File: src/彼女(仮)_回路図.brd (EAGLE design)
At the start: 65.7 x 50 mm, 55 parts, among them IC1 A3921, SW1 TVAF06-A020B-R, SW2 TVAF06-A020B-R, SW3 THAF01-NC-R, SW4 SS-12D00G3

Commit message: first commit
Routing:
- net SA: track 1.81 -> 17.1 mm
- net V5: track 48.1 -> 50.5 mm
- net GND: track 23.3 -> 25.4 mm
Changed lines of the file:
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@@
 <wire x1="49.22" y1="30.84" x2="49.22" y2="31.84" width="0.1524" layer="16"/>
 <wire x1="49.22" y1="30.84" x2="48.98" y2="30.6" width="0.1524" layer="16"/>
+<wire x1="35.84" y1="29.68" x2="35.84" y2="31.7" width="0.1524" layer="16"/>
+<wire x1="35.84" y1="31.7" x2="35.78" y2="31.76" width="0.1524" layer="16"/>
 <wire x1="49.99" y1="38.87" x2="55.8" y2="39.2" width="0" layer="19" extent="16-16"/>
 <wire x1="50.69" y1="44.2" x2="49.99" y2="38.87" width="0" layer="19" extent="16-16"/>
@@
 <wire x1="42.34" y1="23.58" x2="45.11" y2="27.28" width="0" layer="19" extent="1-16"/>
 <wire x1="35.78" y1="31.76" x2="42.68" y2="31.84" width="0" layer="19" extent="16-16"/>
-<wire x1="35.84" y1="29.68" x2="35.78" y2="31.76" width="0" layer="19" extent="16-16"/>
 <wire x1="41.77" y1="39.2" x2="42.68" y2="31.84" width="0" layer="19" extent="16-16"/>
 <wire x1="45.54" y1="4.35" x2="41.7" y2="21.3" width="0" layer="19" extent="16-16"/>
@@
 <wire x1="47.3" y1="32.9" x2="42.34" y2="32.9" width="0.1524" layer="16"/>
 <wire x1="42.34" y1="32.9" x2="41.28" y2="31.84" width="0.1524" layer="16"/>
+<wire x1="37.79" y1="29.68" x2="37.79" y2="31.15" width="0.1524" layer="16"/>
+<wire x1="37.79" y1="31.15" x2="37.18" y2="31.76" width="0.1524" layer="16"/>
 <wire x1="47.82" y1="31.84" x2="55.59" y2="26.01" width="0" layer="19" extent="1-16"/>
 <wire x1="40.61" y1="31.81" x2="41.28" y2="31.84" width="0" layer="19" extent="1-16"/>
@@
 <wire x1="38.44" y1="29.68" x2="39.09" y2="29.68" width="0" layer="19" extent="16-16"/>
 <wire x1="37.79" y1="29.68" x2="38.44" y2="29.68" width="0" layer="19" extent="16-16"/>
-<wire x1="37.18" y1="31.76" x2="37.79" y2="29.68" width="0" layer="19" extent="16-16"/>
 <wire x1="6.59" y1="34.66" x2="37.18" y2="31.76" width="0" layer="19" extent="16-16"/>
 <wire x1="4.41" y1="34.7" x2="6.59" y2="34.66" width="0" layer="19" extent="16-16"/>
@@
 <contactref element="EDGE1" pad="P$3"/>
 <contactref element="EDGE1" pad="P$4"/>
-<wire x1="36.42" y1="21.8" x2="36.42" y2="23.51" width="0.1524" layer="16"/>
+<wire x1="36.42" y1="23.51" x2="36.42" y2="21.8" width="0.1524" layer="16"/>
 <wire x1="36.42" y1="23.51" x2="36.49" y2="23.58" width="0.1524" layer="16"/>
+<wire x1="36.42" y1="21.8" x2="36.42" y2="19.29" width="0.1524" layer="16"/>
+<wire x1="36.42" y1="19.29" x2="35.78" y2="18.65" width="0.1524" layer="16"/>
+<wire x1="35.78" y1="18.65" x2="29.52" y2="18.65" width="0.1524" layer="16"/>
+<wire x1="29.52" y1="18.65" x2="25.58" y2="22.59" width="0.1524" layer="16"/>
 <wire x1="24.29" y1="28.75" x2="11.71" y2="45.72" width="0" layer="19" extent="16-16"/>
 <wire x1="25.58" y1="22.59" x2="24.29" y2="28.75" width="0" layer="19" extent="16-16"/>
-<wire x1="36.42" y1="21.8" x2="25.58" y2="22.59" width="0" layer="19" extent="16-16"/>
 <wire x1="12.59" y1="14.7546" x2="25.58" y2="22.59" width="0" layer="19" extent="1-16"/>
 <wire x1="12.52" y1="4.35" x2="12.59" y2="14.7546" width="0" layer="19" extent="1-16"/>

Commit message: brd編集 配線
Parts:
- moved 3813-HA 4.00 mm to (22.8, 23.7)
- moved 3813-LA 4.00 mm to (8.59, 23.7)
- moved C10 2.00 mm to (39.8, 41.7)
- moved C7 1.30 mm to (40.4, 22.2), flipped to the bottom, turned to 180 degrees
- moved 3813-HB 1.00 mm to (25.3, 33.8)
- moved 3813-LB 1.00 mm to (11.1, 33.8)
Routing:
- net N$11: track 0.00 -> 23.2 mm
- net V5: track 50.5 -> 73.6 mm, vias 2 -> 3
- net SA: track 17.1 -> 1.81 mm
- net GND: track 25.4 -> 33.9 mm
- net N$3: track 0.00 -> 5.76 mm, vias 0 -> 1
- net N$4: track 0.00 -> 5.73 mm
- net N$2: track 0.00 -> 4.73 mm
- net N$1: track 0.00 -> 2.46 mm
- net N$15: track 3.11 -> 1.46 mm, vias 1 -> 0
- net SB: track 3.09 -> 1.44 mm, vias 1 -> 0
- net PWM: track 28.6 -> 29.9 mm
- net N$25: track 0.00 -> 0.61 mm

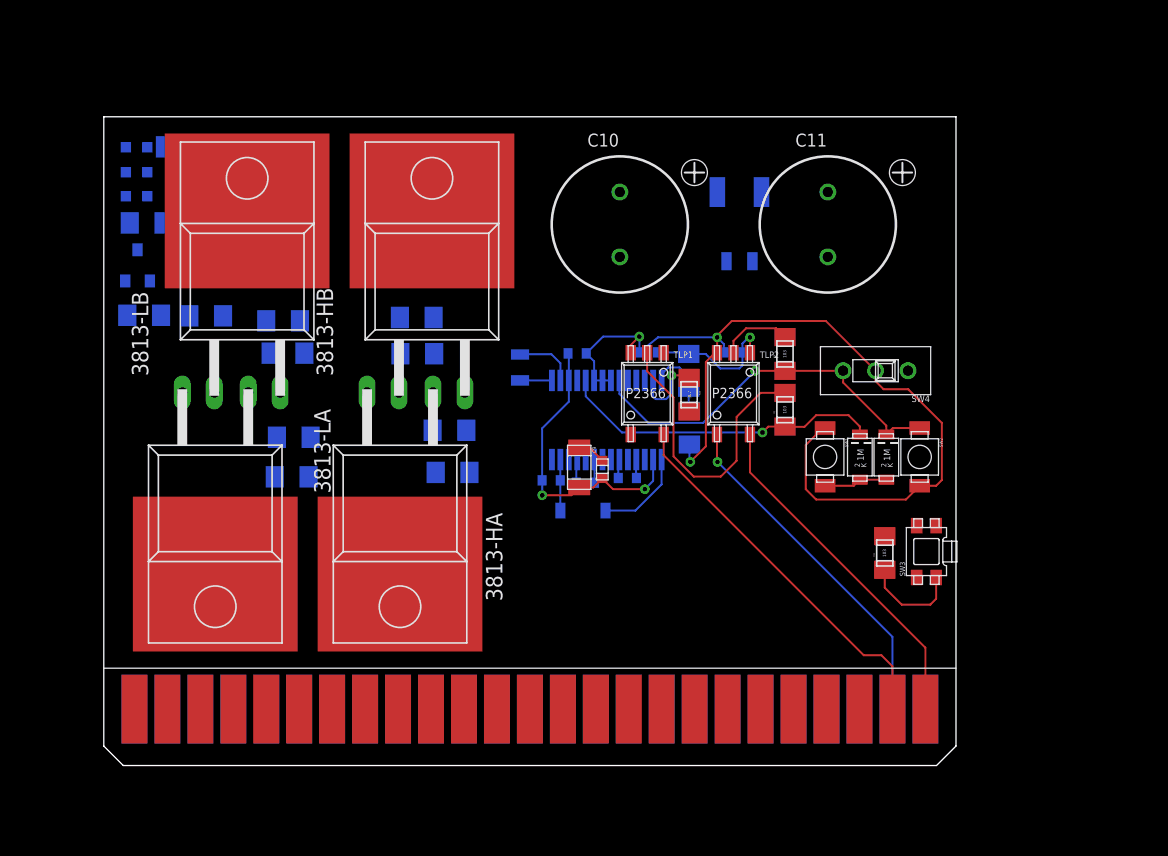
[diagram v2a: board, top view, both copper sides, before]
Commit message: 部品配置訂正 大電流パターン考慮
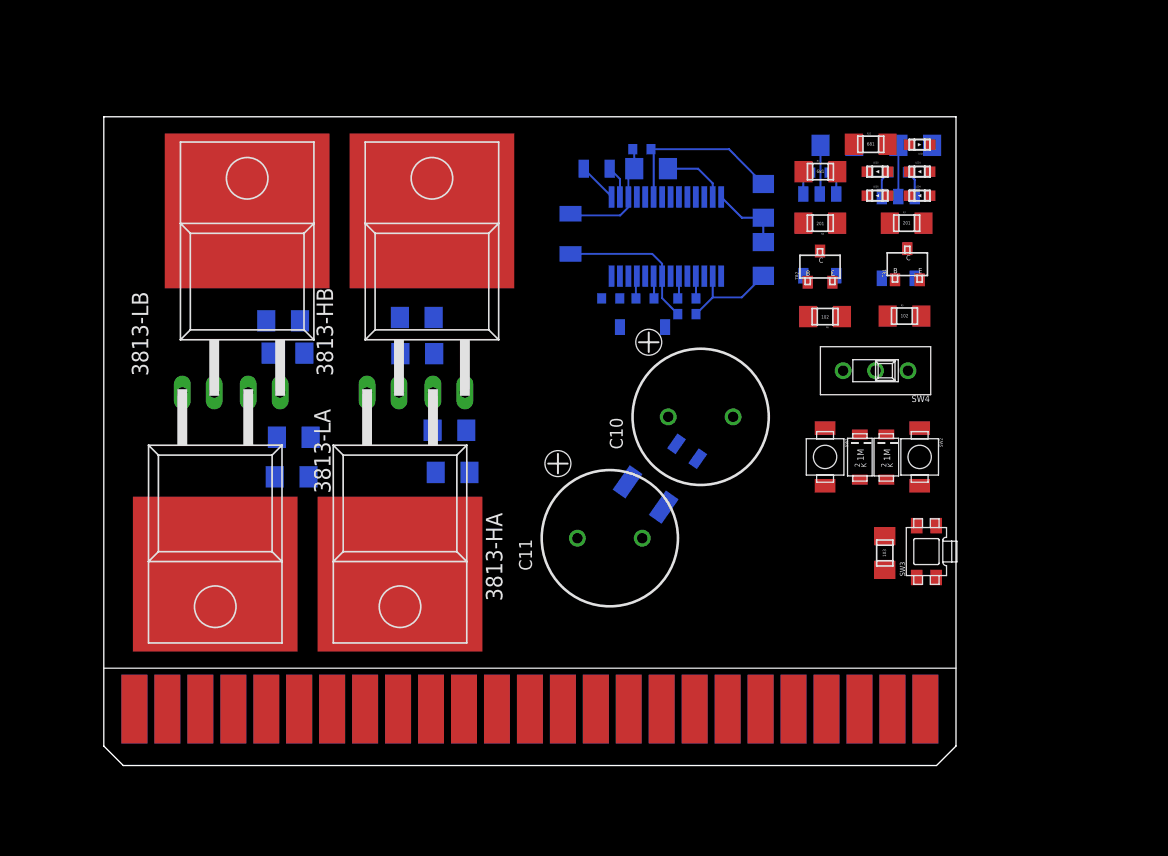
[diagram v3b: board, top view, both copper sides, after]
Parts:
- moved LED3 62.0 mm to (63.7, 47.9), flipped to the top
- moved LED1 60.4 mm to (62.0, 45.8), flipped to the top, turned to 270 degrees
- moved TR1 57.3 mm to (62.9, 37.4), flipped to the top
- moved LED5 57.1 mm to (58.8, 43.9), flipped to the top, turned to 270 degrees
- moved LED4 56.5 mm to (62.0, 43.9), flipped to the top, turned to 270 degrees
- moved TR2 54.5 mm to (56.1, 37.2), flipped to the top
- moved R7 54.4 mm to (60.6, 41.8), flipped to the top, turned to 0 degrees
- moved R5 53.8 mm to (60.4, 34.6), flipped to the top, turned to 0 degrees
- moved LED2 53.3 mm to (58.8, 45.8), flipped to the top, turned to 270 degrees
- moved R6 52.5 mm to (56.9, 34.6), flipped to the top, turned to 180 degrees
- moved R8 51.9 mm to (56.5, 41.8), flipped to the top, turned to 180 degrees
- moved R22 50.5 mm to (57.8, 47.9), flipped to the top
- moved R3 42.2 mm to (53.9, 45.8), flipped to the top
- moved C11 29.4 mm to (39.0, 17.5), turned to 90 degrees
- moved TLP1 25.0 mm to (62.5, 37.5), flipped to the bottom
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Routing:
- net V5: track 73.6 -> 17.5 mm, vias 3 -> 0
- net PWM: track 29.9 -> 0.00 mm, vias 1 -> 0
- net GND_IN: track 29.3 -> 0.00 mm
- net VCC_IN: track 26.8 -> 0.00 mm, vias 1 -> 0
- net PWM_IN: track 26.8 -> 0.00 mm
- net DIR: track 25.1 -> 0.00 mm, vias 1 -> 0
- net N$11: track 23.2 -> 3.95 mm
- net GND: track 33.9 -> 21.5 mm, vias 3 -> 0
- net N$6: track 2.20 -> 11.8 mm
- net RESET: track 7.70 -> 0.00 mm
- net VCC: track 7.07 -> 0.00 mm
- net N$12: track 4.91 -> 0.00 mm
- net N$7: track 3.94 -> 0.00 mm
- net N$2: track 4.73 -> 2.51 mm
- net N$14: track 5.57 -> 3.77 mm
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
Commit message: edit:配線の追加
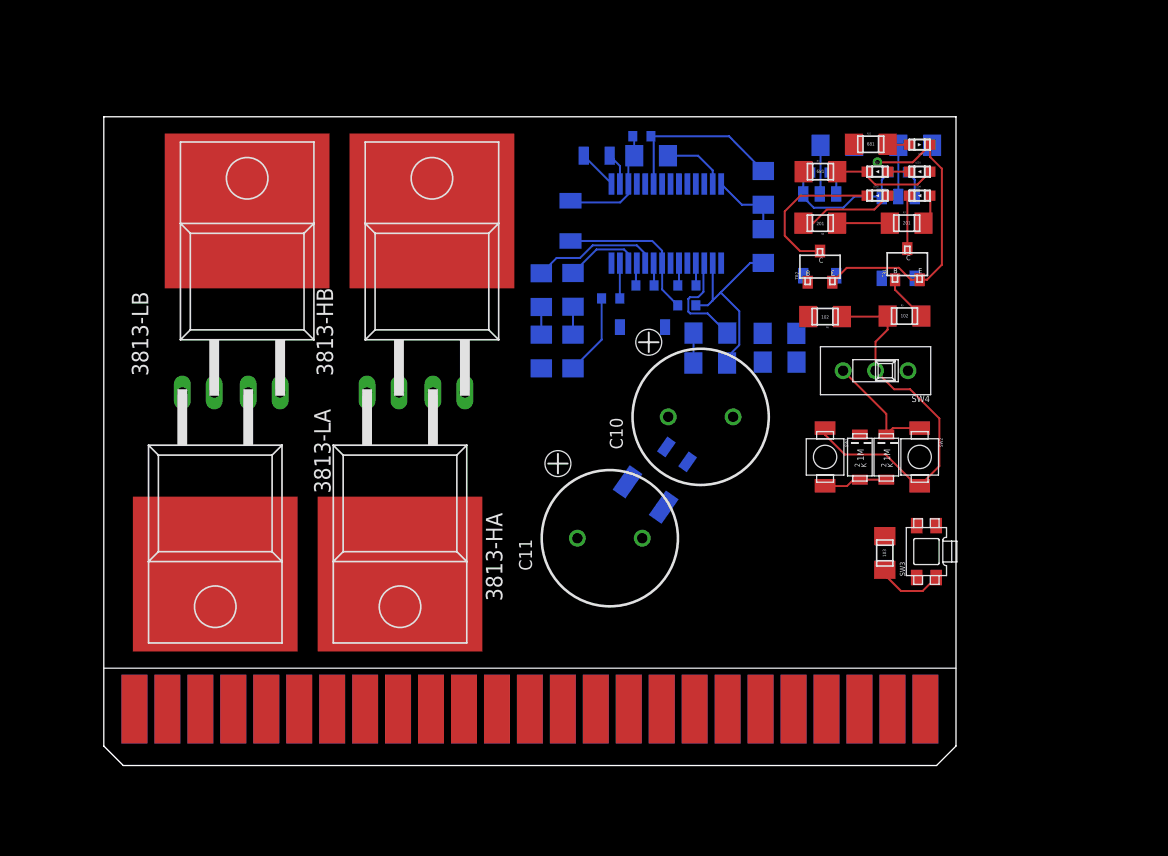
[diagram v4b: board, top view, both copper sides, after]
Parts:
- moved R18 33.1 mm to (48.0, 31.0)
- moved R10 32.6 mm to (48.0, 33.3)
- moved R19 28.2 mm to (53.4, 31.1)
- moved R12 28.0 mm to (53.4, 33.3)
- moved R20 24.9 mm to (36.2, 35.4), turned to 90 degrees
- moved R15 24.5 mm to (36.2, 30.6), turned to 90 degrees
- moved R21 12.7 mm to (33.7, 35.3), turned to 90 degrees
- moved R16 11.4 mm to (33.7, 30.6), turned to 90 degrees
- moved C3 1.00 mm to (41.5, 48.5)
- moved C6 1.00 mm to (38.0, 47.0)
- moved C7 1.00 mm to (44.9, 37.0)
- moved C8 1.00 mm to (41.7, 37.0)
- moved C9 1.00 mm to (36.0, 42.0)
- moved IC1 1.00 mm to (47.6, 39.6)
- moved R13 1.00 mm to (43.5, 47.0)
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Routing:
- net GND: track 21.5 -> 67.9 mm, vias 0 -> 1
- net V5: track 17.5 -> 51.4 mm
- net N$8: track 0.00 -> 11.9 mm
- net GHA: track 0.00 -> 9.89 mm
- net PWM: track 0.00 -> 9.08 mm
- net GLB: track 0.00 -> 8.56 mm
- net N$18: track 0.00 -> 8.19 mm
- net N$10: track 0.00 -> 7.41 mm
- net GLA: track 0.00 -> 5.88 mm
- net RESET: track 0.00 -> 5.29 mm
- net N$12: track 0.00 -> 5.26 mm
- net N$5: track 0.00 -> 4.13 mm
- net N$19: track 0.00 -> 3.64 mm
- net N$7: track 0.00 -> 2.72 mm
- net N$9: track 0.00 -> 2.34 mm
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
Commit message: edit:GND,VCCベタ,wireの追加
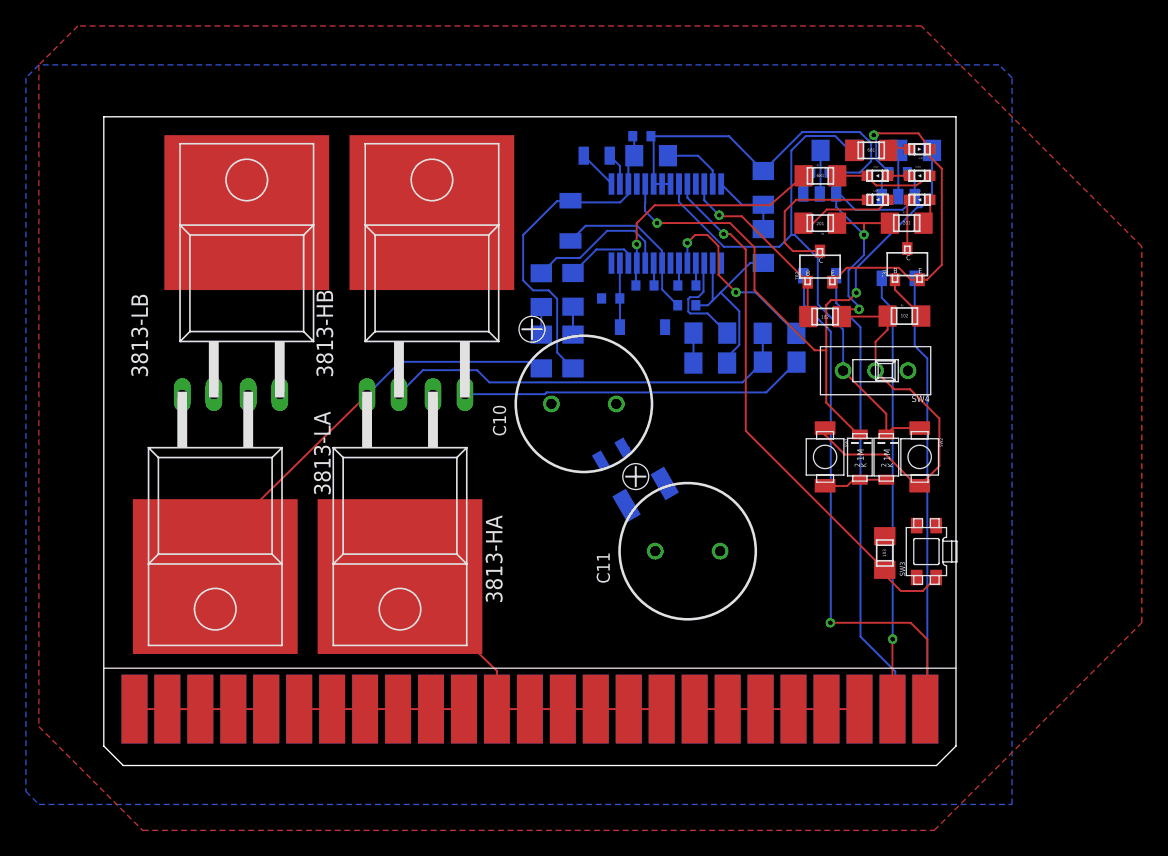
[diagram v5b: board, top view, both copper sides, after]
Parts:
- moved C10 9.06 mm to (37.0, 27.9)
- moved C11 6.08 mm to (45.0, 16.5)
- moved C13 5.00 mm to (39.2, 24.0), turned to 150 degrees
- moved R22 0.47 mm to (57.9, 47.4)
- moved R1 0.39 mm to (63.8, 47.4)
- moved R9 0.39 mm to (57.8, 47.4)
- moved LED3 0.35 mm to (63.7, 47.5)
- moved LED5 0.32 mm to (58.8, 43.6)
- moved LED1 0.32 mm to (62.0, 45.5)
- moved LED2 0.32 mm to (58.8, 45.5)
- moved LED4 0.32 mm to (62.0, 43.6)
- moved R3 0.32 mm to (53.9, 45.5)
- moved 3813-HA 0.19 mm to (22.8, 23.5)
- moved 3813-LA 0.19 mm to (8.59, 23.5)
- moved 3813-LB 0.13 mm to (11.0, 33.7)
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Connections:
- removed net N$19: R5.RIGHT, TR1.B
- removed net N$20: R6.RIGHT, TR2.B
- net FF1: now also R5.RIGHT, TR1.B
- net FF2: now also R6.RIGHT, TR2.B
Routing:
- net SA: track 1.75 -> 62.9 mm, vias 0 -> 1
- net DIR: track 0.00 -> 49.9 mm, vias 0 -> 2
- net PWM_IN: track 0.00 -> 43.4 mm, vias 0 -> 1
- net SB: track 3.32 -> 42.6 mm
- net V5: track 51.4 -> 87.8 mm, vias 0 -> 2
- net RESET: track 5.29 -> 41.6 mm, vias 0 -> 1
- net PWM: track 9.08 -> 45.4 mm
- net VCC_IN: track 0.00 -> 35.4 mm
- net DIR_IN: track 0.00 -> 33.7 mm
- net GND_IN: track 0.00 -> 33.6 mm, vias 0 -> 1
- net N$21: track 0.00 -> 32.1 mm
- net VCC: track 0.30 -> 26.1 mm
- net GND: track 67.9 -> 89.9 mm
- net GHB: track 0.00 -> 14.7 mm, vias 0 -> 2
- net FF2: track 0.00 -> 14.6 mm, vias 0 -> 1
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- added copper zone on layer 16, net GND
- added copper zone on layer 1, net VCC

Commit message: edit:大体配線完了
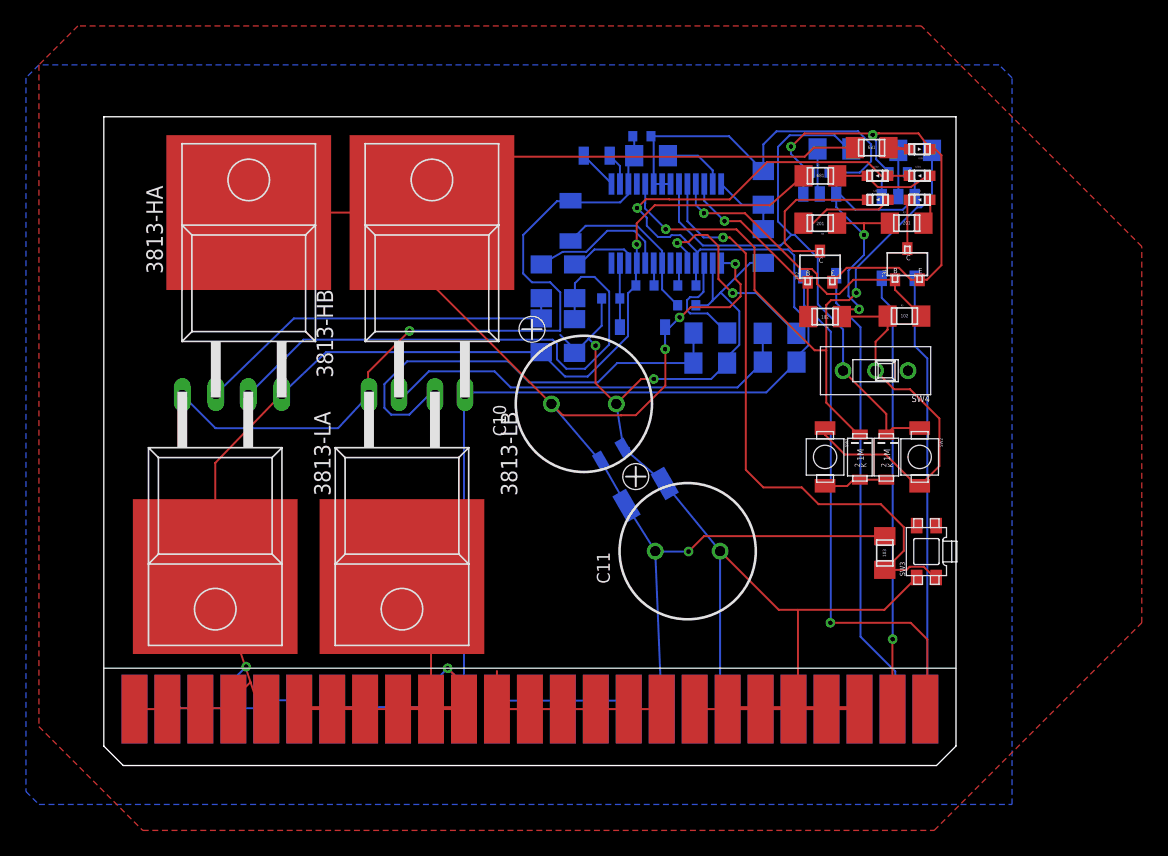
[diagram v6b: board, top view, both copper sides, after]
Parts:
- moved 3813-LB 15.7 mm to (23.0, 23.5), turned to 180 degrees
- moved 3813-HA 15.5 mm to (11.2, 33.7), turned to 0 degrees
- moved R16 1.25 mm to (33.7, 31.9)
- moved R15 1.20 mm to (36.3, 31.8)
- moved R21 0.68 mm to (33.7, 36.0)
- moved R20 0.67 mm to (36.3, 36.0)
- moved R9 0.25 mm to (57.6, 47.5)
- moved R22 0.21 mm to (57.9, 47.6)
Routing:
- net VCC: track 26.1 -> 179.6 mm, vias 0 -> 4
- net GND: track 89.9 -> 229.0 mm, vias 1 -> 5
- net SB: track 42.6 -> 154.0 mm, vias 0 -> 2
- net SA: track 62.9 -> 115.2 mm, vias 1 -> 2
- net N$25: track 2.15 -> 42.2 mm
- net N$26: track 2.31 -> 34.7 mm
- net N$13: track 2.13 -> 29.0 mm
- net FF1: track 3.64 -> 24.3 mm, vias 0 -> 1
- net RESET: track 41.6 -> 47.8 mm
- net PWM: track 45.4 -> 47.6 mm
- net V5: track 87.8 -> 89.6 mm
- net N$22: track 1.62 -> 3.29 mm
- net GHB: track 14.7 -> 16.0 mm

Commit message: ビアの配置
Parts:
- moved 3813-HA 1.10 mm to (11.2, 34.8)
- moved 3813-HB 1.10 mm to (25.3, 34.8)
- moved 3813-LA 1.08 mm to (8.59, 24.6)
- moved 3813-LB 1.08 mm to (23.0, 24.6)
- moved R18 1.00 mm to (48.0, 32.0)
- moved R19 1.00 mm to (53.4, 32.1)
- moved C1 1.00 mm to (61.2, 46.7)
- moved C10 1.00 mm to (37.0, 28.9)
- moved C11 1.00 mm to (45.0, 17.5)
- moved C12 1.00 mm to (41.8, 21.9)
- moved C13 1.00 mm to (39.2, 25.0)
- moved C2 1.00 mm to (55.2, 46.7)
- moved C3 1.00 mm to (41.5, 49.5)
- moved C4 1.00 mm to (44.9, 36.5)
- moved C5 1.00 mm to (39.1, 37.0)
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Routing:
- net SA: track 115.2 -> 53.4 mm, vias 2 -> 123
- net SB: track 154.0 -> 98.1 mm, vias 2 -> 1
- net GND: track 229.0 -> 173.4 mm
- net VCC: track 179.6 -> 125.6 mm
- net VCC_IN: track 35.4 -> 36.4 mm
- net PWM_IN: track 43.4 -> 44.4 mm
- net GND_IN: track 33.6 -> 34.6 mm
- net DIR_IN: track 33.7 -> 34.7 mm
- net N$26: track 34.7 -> 35.3 mm
- added copper zone on layer 1, net SA
- added copper zone on layer 16, net SA
- added copper zone on layer 1, net SB
- added copper zone on layer 16, net SB
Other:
- board size 65.7 x 50 mm -> 65.7 x 51 mm

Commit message: ビア,パターンの追加 ほぼ完成
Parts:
- moved C12 2.99 mm to (43.3, 24.5), turned to 135 degrees
- moved C13 1.90 mm to (40.6, 26.2), turned to 135 degrees
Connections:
- net GND: now also EDGE1.P$34, EDGE1.P$35, EDGE1.P$36, EDGE1.P$37, EDGE1.P$38, EDGE1.P$39; no longer EDGE1.P$18, EDGE1.P$19, EDGE1.P$20, EDGE1.P$21, EDGE1.P$22, EDGE1.P$23
- net VCC: now also EDGE1.P$18, EDGE1.P$19, EDGE1.P$20, EDGE1.P$21, EDGE1.P$22, EDGE1.P$23; no longer EDGE1.P$34, EDGE1.P$35, EDGE1.P$36, EDGE1.P$37, EDGE1.P$38, EDGE1.P$39
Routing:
- net VCC: track 125.6 -> 78.4 mm, vias 4 -> 126
- net GND: track 173.4 -> 138.6 mm, vias 5 -> 6
- net N$13: track 29.0 -> 30.5 mm
- net N$25: track 42.1 -> 43.4 mm
- net SB: vias 1 -> 123
- added copper zone on layer 16, net VCC
